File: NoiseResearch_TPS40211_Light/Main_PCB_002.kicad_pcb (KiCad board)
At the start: 2 copper layers, 37.3 x 20.1 mm, 42 parts, among them IC1 TPS40211QDGQRQ1, Q1 AON7407, U12 MCP9700AT-ETT, U13 MCP9700AT-ETT, U2 Mounting_Hole_M2, U3 Mounting_Hole_M2, U4 Mounting_Hole_M2, U5 Mounting_Hole_M2

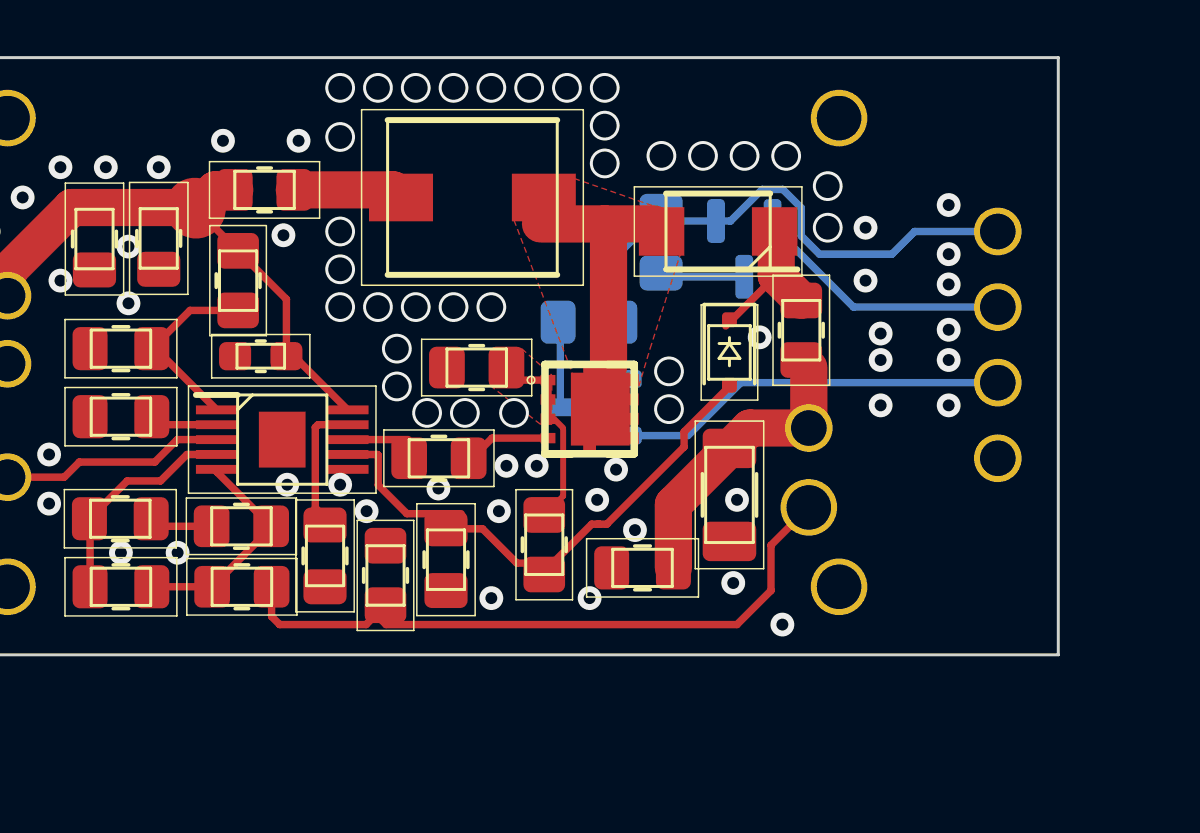
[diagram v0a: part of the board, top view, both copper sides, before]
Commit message: Noise research for TSP40211 005
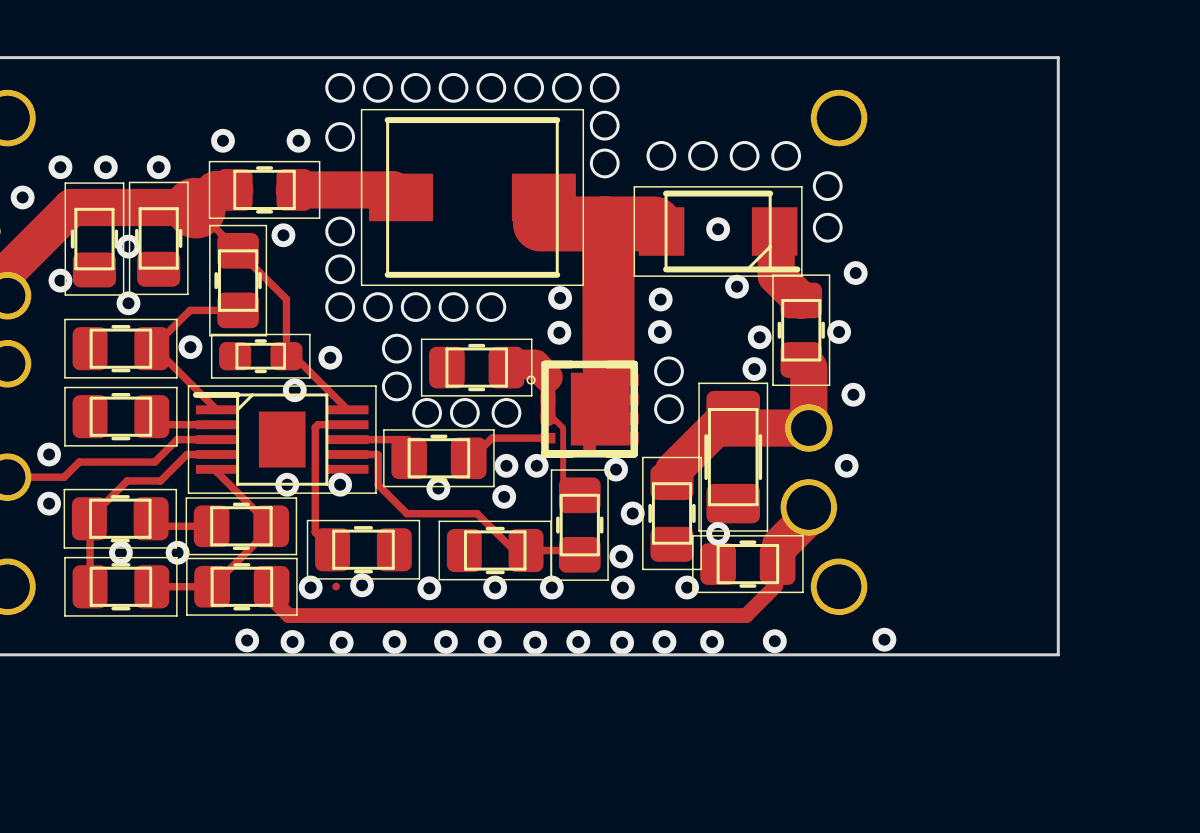
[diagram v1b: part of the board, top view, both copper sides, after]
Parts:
- removed C49, C50: C, Capacitor_SMD:C_0805_2012Metric_Pad1.18x1.45mm_HandSolder
- removed D66: +5B, libraries:WireHole_1p2
- removed D67: t_D, libraries:WireHole_1p2
- removed D68: t_Q, libraries:WireHole_1p2
- removed D69: Gnd, libraries:WireHole_1p2
- removed U12, U13: MCP9700AT-ETT, Package_TO_SOT_SMD:SOT-23
- removed Z1: BZT52-C5V1J, Diode_SMD:D_SOD-323F
- moved R1 12.2 mm to (126.5, 137.7), turned to 0 degrees
- moved C30 2.08 mm to (123.9, 136.0), turned to -90 degrees
- moved C11 1.68 mm to (118.0, 137.2), turned to 180 degrees
- moved R7 1.36 mm to (120.8, 136.4)
- moved C9 1.31 mm to (113.6, 137.2), turned to 0 degrees
- moved C13 1.28 mm to (126.0, 134.1)
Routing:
- net Net-(D66-Conn): track 19.6 -> 0.00 mm
- net Net-(D67-Conn): track 13.4 -> 0.00 mm
- net Net-(D68-Conn): track 8.87 -> 0.00 mm
- net Net-(IC1-ISNS): track 17.4 -> 9.78 mm
- net GND: track 5.77 -> 0.02 mm, vias 73 -> 91
- net Net-(D6-Conn): track 22.8 -> 19.6 mm
- net Net-(D12-Pad1): track 5.45 -> 3.05 mm
- net Net-(D10-Conn): track 10.1 -> 8.28 mm
- net Net-(IC1-BP): track 4.65 -> 5.48 mm
- net Net-(Q1-S_1): track 6.52 -> 5.88 mm
- removed copper zone on F.Cu, net Net-(Q1-D_1)
- removed copper zone on F.Cu, net Net-(Q1-S_1)

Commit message: BANO Step-Dn 001
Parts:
- moved R6 0.99 mm to (117.1, 134.1)
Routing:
- net Net-(IC1-GDRV): track 2.04 -> 3.29 mm
- net Net-(Q1-G): track 2.83 -> 1.88 mm
- net GND: vias 91 -> 92
